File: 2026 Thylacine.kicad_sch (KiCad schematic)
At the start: 0 parts

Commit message: Jonathan's PDH, swerve, and top-level graphics
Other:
- sheet Swerve Module 0 renamed Swerve Module FRONT RIGHT
- sheet Swerve Module 1 renamed Swerve Module BOTTOM RIGHT
- sheet Swerve Module 2 renamed Swerve Module FRONT LEFT
- sheet Swerve Module 3 renamed Swerve Module BOTTOM LEFT
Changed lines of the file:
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@@
 	(paper "A4")
 	(sheet
-		(at 200.66 43.18)
-		(size 50.8 53.34)
+		(at 127 76.2)
+		(size 50.8 50.8)
 		(exclude_from_sim no)
 		(in_bom yes)
@@
 		)
 		(property "Sheetname" "Power Distribution"
-			(at 200.66 42.4684 0)
+			(at 127 75.4884 0)
 			(effects
 				(font
@@
 		)
 		(property "Sheetfile" "PDH.kicad_sch"
-			(at 200.66 97.1046 0)
+			(at 127 127.5846 0)
 			(effects
 				(font
@@
 	)
 	(sheet
-		(at 186.69 118.11)
+		(at 13.97 167.64)
 		(size 50.8 25.4)
 		(exclude_from_sim no)
@@
 		)
 		(property "Sheetname" "Intake Motors"
-			(at 186.69 117.3984 0)
+			(at 13.97 166.9284 0)
 			(effects
 				(font
@@
 		)
 		(property "Sheetfile" "Intake.kicad_sch"
-			(at 186.69 144.0946 0)
+			(at 13.97 193.6246 0)
 			(effects
 				(font
@@
 	)
 	(sheet
-		(at 139.7 44.45)
-		(size 17.78 11.43)
-		(exclude_from_sim no)
-		(in_bom yes)
-		(on_board yes)
-		(dnp no)
-		(fields_autoplaced yes)
+		(at 139.7 25.4)
+		(size 25.4 25.4)
+		(exclude_from_sim no)
+		(in_bom yes)
+		(on_board yes)
+		(dnp no)
 		(stroke
 			(width 0.1524)
@@
 		)
 		(property "Sheetname" "RoboRio"
-			(at 139.7 43.7384 0)
+			(at 139.7 24.13 0)
 			(effects
 				(font
@@
 		)
 		(property "Sheetfile" "roborio.kicad_sch"
-			(at 139.7 56.4646 0)
+			(at 139.7 51.3846 0)
 			(effects
 				(font
@@
 	)
 	(sheet
-		(at 57.15 27.94)
-		(size 12.7 7.62)
-		(exclude_from_sim no)
-		(in_bom yes)
-		(on_board yes)
-		(dnp no)
-		(fields_autoplaced yes)
-		(stroke
-			(width 0.1524)
-			(type solid)
-		)
-		(fill
-			(color 0 0 0 0.0000)
-		)
-		(property "Sheetname" "Swerve Module 0"
-			(at 57.15 27.2284 0)
-			(effects
-				(font
-					(size 1.27 1.27)
-				)
-				(justify left bottom)
-			)
-		)
-		(property "Sheetfile" "Swerve0.kicad_sch"
-			(at 57.15 36.1446 0)
+		(at 203.2 38.1)
+		(size 12.7 12.7)
+		(exclude_from_sim no)
+		(in_bom yes)
+		(on_board yes)
+		(dnp no)
+		(stroke
+			(width 0.1524)
+			(type solid)
+		)
+		(fill
+			(color 0 0 0 0.0000)
+		)
+		(property "Sheetname" "Swerve Module FRONT RIGHT"
+			(at 203.2 36.83 0)
+			(effects
+				(font
+					(size 1.27 1.27)
+				)
+				(justify left bottom)
+			)
+		)
+		(property "Sheetfile" "Swerve0.kicad_sch"
+			(at 203.2 51.3846 0)
 			(effects
 				(font
@@
 	)
 	(sheet
-		(at 38.1 50.8)
-		(size 12.7 7.62)
-		(exclude_from_sim no)
-		(in_bom yes)
-		(on_board yes)
-		(dnp no)
-		(fields_autoplaced yes)
-		(stroke
-			(width 0.1524)
-			(type solid)
-		)
-		(fill
-			(color 0 0 0 0.0000)
-		)
-		(property "Sheetname" "Swerve Module 1"
-			(at 38.1 50.0884 0)
-			(effects
-				(font
-					(size 1.27 1.27)
-				)
-				(justify left bottom)
-			)
-		)
-		(property "Sheetfile" "Swerve0.kicad_sch"
-			(at 38.1 59.0046 0)
+		(at 203.2 152.4)
+		(size 12.7 12.7)
+		(exclude_from_sim no)
+		(in_bom yes)
+		(on_board yes)
+		(dnp no)
+		(stroke
+			(width 0.1524)
+			(type solid)
+		)
+		(fill
+			(color 0 0 0 0.0000)
+		)
+		(property "Sheetname" "Swerve Module BOTTOM RIGHT"
+			(at 203.2 151.13 0)
+			(effects
+				(font
+					(size 1.27 1.27)
+				)
+				(justify left bottom)
+			)
+		)
+		(property "Sheetfile" "Swerve0.kicad_sch"
+			(at 203.2 165.6846 0)
 			(effects
 				(font
@@
 	)
 	(sheet
-		(at 38.1 100.33)
-		(size 12.7 7.62)
-		(exclude_from_sim no)
-		(in_bom yes)
-		(on_board yes)
-		(dnp no)
-		(fields_autoplaced yes)
-		(stroke
-			(width 0.1524)
-			(type solid)
-		)
-		(fill
-			(color 0 0 0 0.0000)
-		)
-		(property "Sheetname" "Swerve Module 3"
-			(at 38.1 99.6184 0)
-			(effects
-				(font
-					(size 1.27 1.27)
-				)
-				(justify left bottom)
-			)
-		)
-		(property "Sheetfile" "Swerve0.kicad_sch"
-			(at 38.1 108.5346 0)
+		(at 88.9 152.4)
+		(size 12.7 12.7)
+		(exclude_from_sim no)
+		(in_bom yes)
+		(on_board yes)
+		(dnp no)
+		(stroke
+			(width 0.1524)
+			(type solid)
+		)
+		(fill
+			(color 0 0 0 0.0000)
+		)
+		(property "Sheetname" "Swerve Module BOTTOM LEFT"
+			(at 88.9 151.13 0)
+			(effects
+				(font
+					(size 1.27 1.27)
+				)
+				(justify left bottom)
+			)
+		)
+		(property "Sheetfile" "Swerve0.kicad_sch"
+			(at 88.9 165.6846 0)
 			(effects
 				(font
@@
 	)
 	(sheet
-		(at 39.37 77.47)
-		(size 12.7 7.62)
-		(exclude_from_sim no)
-		(in_bom yes)
-		(on_board yes)
-		(dnp no)
-		(fields_autoplaced yes)
-		(stroke
-			(width 0.1524)
-			(type solid)
-		)
-		(fill
-			(color 0 0 0 0.0000)
-		)
-		(property "Sheetname" "Swerve Module 2"
-			(at 39.37 76.7584 0)
-			(effects
-				(font
-					(size 1.27 1.27)
-				)
-				(justify left bottom)
-			)
-		)
-		(property "Sheetfile" "Swerve0.kicad_sch"
-			(at 39.37 85.6746 0)
-			(effects
-				(font
+		(at 88.9 38.1)
+		(size 12.7 12.7)
+		(exclude_from_sim no)
+		(in_bom yes)
+		(on_board yes)
+		(dnp no)
+		(stroke
+			(width 0.1524)
+			(type solid)
+		)
+		(fill
+			(color 0 0 0 0.0000)
+		)
+		(property "Sheetname" "Swerve Module FRONT LEFT"
+			(at 88.9 36.83 0)
+			(effects
+				(font
+					(size 1.27 1.27)
+				)
+				(justify left bottom)
+			)
+		)
+		(property "Sheetfile" "Swerve0.kicad_sch"
+			(at 88.9 51.3846 0)
+			(effects
+				(font

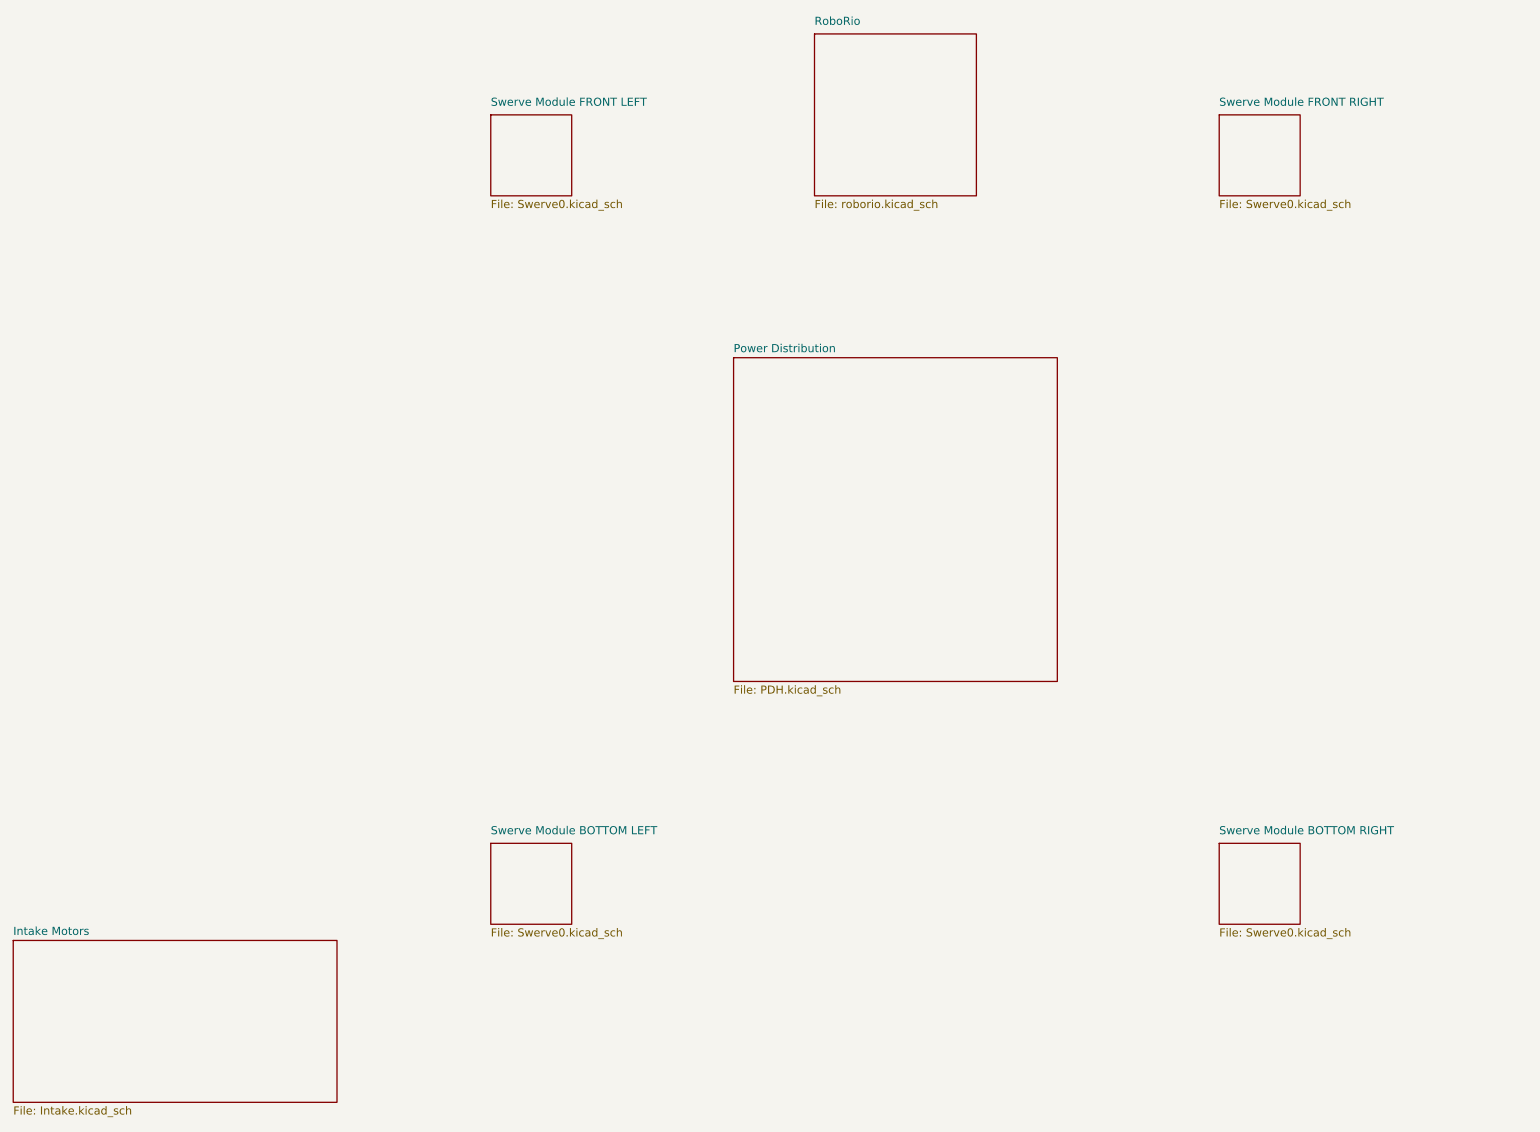
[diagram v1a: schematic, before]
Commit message: Jonathan: Completed roborio, swerve, and top level schematics Added and wired radio
Jeremy:
Fixed unnamed radio file

Signed-off-by: Jeremy Siegfried <jeremy.siegfried@howlandschools.org>
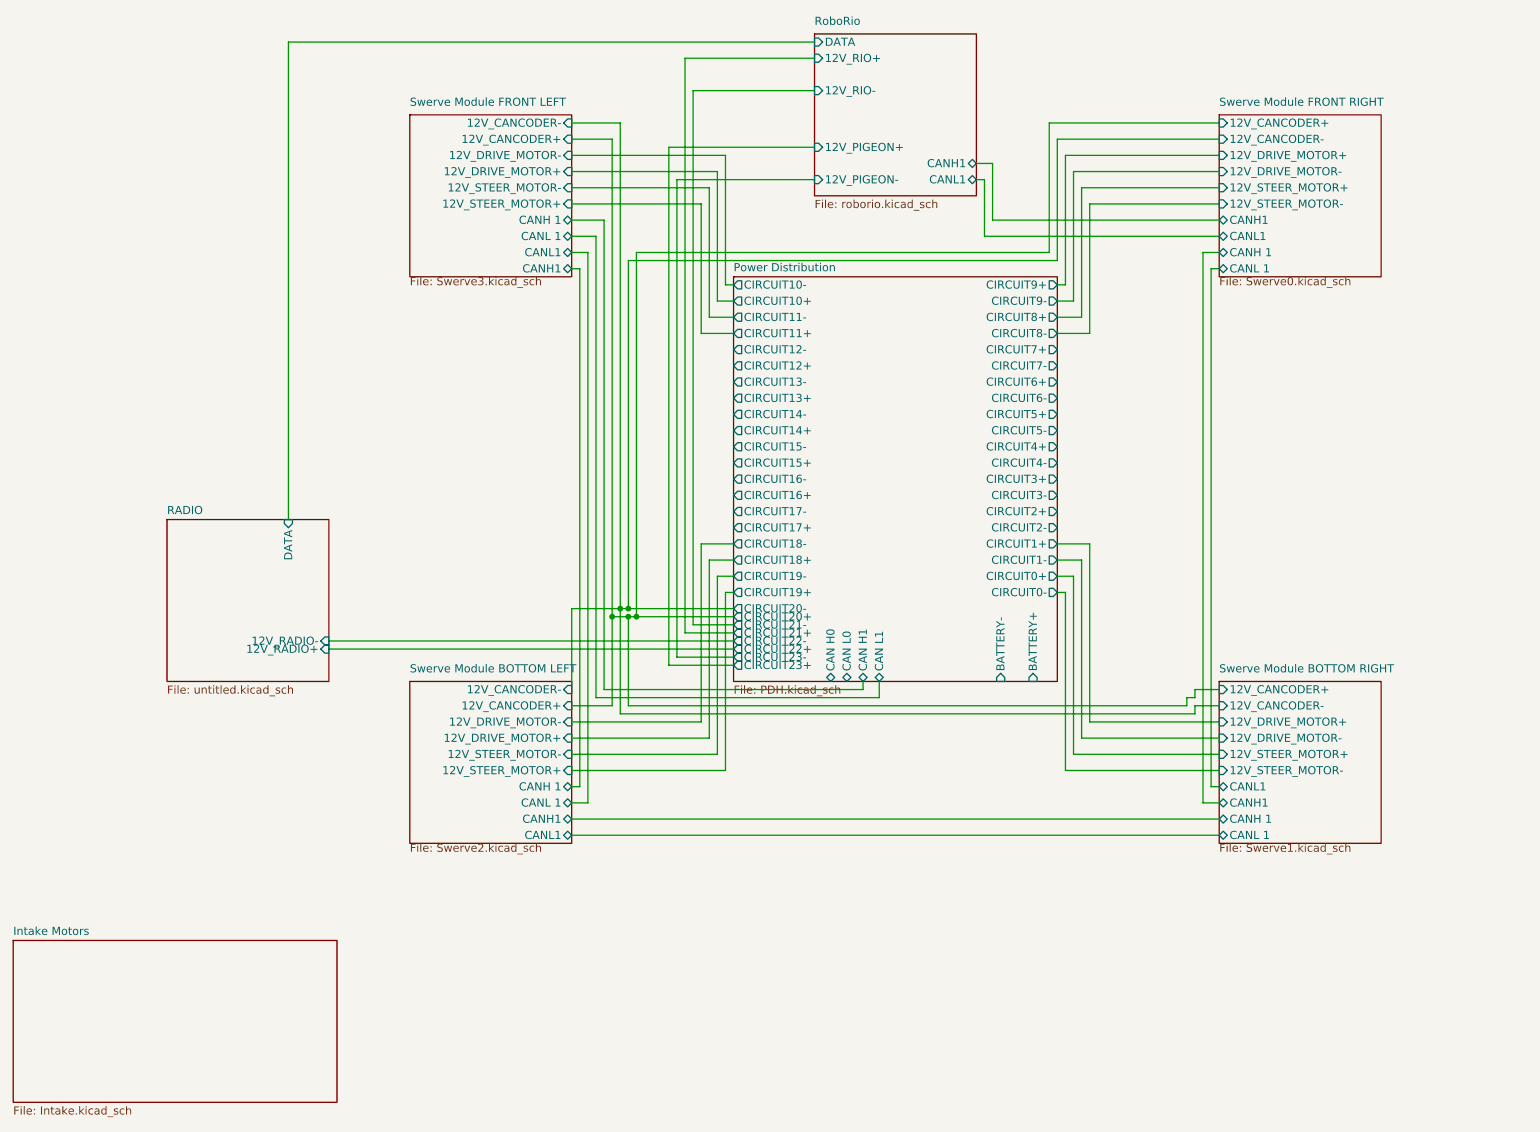
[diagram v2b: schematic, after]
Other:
- added sheet RADIO (untitled.kicad_sch)
- sheet Power Distribution ports: added BATTERY+, BATTERY-, CAN H0, CAN H1, CAN L0, CAN L1, CIRCUIT0+, CIRCUIT0-, CIRCUIT1+, CIRCUIT1-, CIRCUIT10+, CIRCUIT10-, CIRCUIT11+, CIRCUIT11-, CIRCUIT12+, CIRCUIT12-, CIRCUIT13+, CIRCUIT13-, CIRCUIT14+, CIRCUIT14-, CIRCUIT15+, CIRCUIT15-, CIRCUIT16+, CIRCUIT16-, CIRCUIT17+, CIRCUIT17-, CIRCUIT18+, CIRCUIT18-, CIRCUIT19+, CIRCUIT19-, CIRCUIT2+, CIRCUIT2-, CIRCUIT20+, CIRCUIT20-, CIRCUIT21+, CIRCUIT21-, CIRCUIT22+, CIRCUIT22-, CIRCUIT23+, CIRCUIT23-, CIRCUIT3+, CIRCUIT3-, CIRCUIT4+, CIRCUIT4-, CIRCUIT5+, CIRCUIT5-, CIRCUIT6+, CIRCUIT6-, CIRCUIT7+, CIRCUIT7-, CIRCUIT8+, CIRCUIT8-, CIRCUIT9+, CIRCUIT9-; removed none
- sheet RoboRio ports: added 12V_PIGEON+, 12V_PIGEON-, 12V_RIO+, 12V_RIO-, CANH1, CANL1, DATA; removed none
- sheet Swerve Module BOTTOM LEFT: file Swerve0.kicad_sch -> Swerve2.kicad_sch
- sheet Swerve Module BOTTOM LEFT ports: added 12V_CANCODER+, 12V_CANCODER-, 12V_DRIVE_MOTOR+, 12V_DRIVE_MOTOR-, 12V_STEER_MOTOR+, 12V_STEER_MOTOR-, CANH 1, CANH1, CANL 1, CANL1; removed none
- sheet Swerve Module BOTTOM RIGHT: file Swerve0.kicad_sch -> Swerve1.kicad_sch
- sheet Swerve Module BOTTOM RIGHT ports: added 12V_CANCODER+, 12V_CANCODER-, 12V_DRIVE_MOTOR+, 12V_DRIVE_MOTOR-, 12V_STEER_MOTOR+, 12V_STEER_MOTOR-, CANH 1, CANH1, CANL 1, CANL1; removed none
- sheet Swerve Module FRONT LEFT: file Swerve0.kicad_sch -> Swerve3.kicad_sch
- sheet Swerve Module FRONT LEFT ports: added 12V_CANCODER+, 12V_CANCODER-, 12V_DRIVE_MOTOR+, 12V_DRIVE_MOTOR-, 12V_STEER_MOTOR+, 12V_STEER_MOTOR-, CANH 1, CANH1, CANL 1, CANL1; removed none
- sheet Swerve Module FRONT RIGHT ports: added 12V_CANCODER+, 12V_CANCODER-, 12V_DRIVE_MOTOR+, 12V_DRIVE_MOTOR-, 12V_STEER_MOTOR+, 12V_STEER_MOTOR-, CANH 1, CANH1, CANL 1, CANL1; removed none
